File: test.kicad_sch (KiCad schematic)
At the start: 85 parts

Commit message: added symmetric voltage and input stage
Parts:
- added U?: LM27762, Package_SON:WSON-12-1EP_3x2mm_P0.5mm_EP1x2.65_ThermalVias, symbol Regulator_SwitchedCapacitor:LM27762
- C1, C2, C4: value (none) -> 1u; footprint (none) -> Capacitor_SMD:C_0805_2012Metric_Pad1.18x1.45mm_HandSolder
- C10, C11, C12, C13, C16, C17, C22, C23, C26, C27, C8, C9: value (none) -> 10u; footprint (none) -> Capacitor_SMD:C_0805_2012Metric_Pad1.18x1.45mm_HandSolder
- C14, C15, C18, C19, C20, C21, C24, C25, C28, C29, C7: value (none) -> 0.1u; footprint (none) -> Capacitor_SMD:C_0805_2012Metric_Pad1.18x1.45mm_HandSolder
- C3, C6: value (none) -> 4u7; footprint (none) -> Capacitor_SMD:C_0805_2012Metric_Pad1.18x1.45mm_HandSolder
- C30: value (none) -> 25p var; footprint (none) -> project_library:JZ300
- C31: value (none) -> 47n; footprint (none) -> Capacitor_SMD:C_0805_2012Metric_Pad1.18x1.45mm_HandSolder
- C32, C33: value (none) -> 100n; footprint (none) -> Capacitor_SMD:C_0805_2012Metric_Pad1.18x1.45mm_HandSolder
- C34: value (none) -> 1p; footprint (none) -> Capacitor_SMD:C_0805_2012Metric_Pad1.18x1.45mm_HandSolder
- C35: value (none) -> 5.5p-30p var; footprint (none) -> project_library:JZ300
- C5: value (none) -> 22u; footprint (none) -> Capacitor_SMD:C_0805_2012Metric_Pad1.18x1.45mm_HandSolder
- D1: value (none) -> LOW_BATTERY; footprint (none) -> LED_SMD:LED_0805_2012Metric_Pad1.15x1.40mm_HandSolder
- D2: value (none) -> LED_ValidSource; footprint (none) -> LED_SMD:LED_0805_2012Metric_Pad1.15x1.40mm_HandSolder
- D3: value (none) -> LED_Charging; footprint (none) -> LED_SMD:LED_0805_2012Metric_Pad1.15x1.40mm_HandSolder
- IC1: value (none) -> LC709203FQH-01TWG
- IC2: value (none) -> BQ24074RGTR
- IC3: value (none) -> USBLC6-2SC6
- IC4: value (none) -> ESP32-S3-WROOM-1-N16
- IC5, IC6: value (none) -> MCP6S91-E_MS
- IC7, IC8: value (none) -> MCP4726A1T-E_CH
- J1: value (none) -> UART0; footprint (none) -> Connector_PinHeader_2.54mm:PinHeader_1x04_P2.54mm_Vertical
- J2, J3: value (none) -> 73100-0105
- JP1: value (none) -> Jumper_3_Open; footprint (none) -> Connector_PinHeader_2.54mm:PinHeader_1x03_P2.54mm_Vertical
- K1, K2: value (none) -> AQY210EHA
- R1, R7, R8: value (none) -> 1k5; footprint (none) -> Resistor_SMD:R_0805_2012Metric_Pad1.20x1.40mm_HandSolder
- R10: value (none) -> 39; footprint (none) -> Resistor_SMD:R_0805_2012Metric_Pad1.20x1.40mm_HandSolder
- R11, R13: value (none) -> 5k; footprint (none) -> Resistor_SMD:R_0805_2012Metric_Pad1.20x1.40mm_HandSolder
- R12: value (none) -> 120; footprint (none) -> Resistor_SMD:R_0805_2012Metric_Pad1.20x1.40mm_HandSolder
- R14, R15: value (none) -> 470; footprint (none) -> Resistor_SMD:R_0805_2012Metric_Pad1.20x1.40mm_HandSolder
- R16, R17, R2, R4, R9: value (none) -> 5k1; footprint (none) -> Resistor_SMD:R_0805_2012Metric_Pad1.20x1.40mm_HandSolder
- R18, R19, R5: value (none) -> 1k; footprint (none) -> Resistor_SMD:R_0805_2012Metric_Pad1.20x1.40mm_HandSolder
- R20, R21: value (none) -> 165k; footprint (none) -> Resistor_SMD:R_0805_2012Metric_Pad1.20x1.40mm_HandSolder
- R22, R23: value (none) -> 835k; footprint (none) -> Resistor_SMD:R_0805_2012Metric_Pad1.20x1.40mm_HandSolder
- R3: value (none) -> 10k; footprint (none) -> Resistor_SMD:R_0805_2012Metric_Pad1.20x1.40mm_HandSolder
- R6: value (none) -> 820; footprint (none) -> Resistor_SMD:R_0805_2012Metric_Pad1.20x1.40mm_HandSolder
- SW1: value (none) -> Reset; footprint (none) -> project_library:SW_TS-1187A-B-A-B
- SW2: value (none) -> Boot
- U1, U2: value (none) -> 1043
- U3: value (none) -> USB-TYPE-C-018
- U4, U5, U6: value (none) -> LD1086DT33TR
- U7, U8: value (none) -> ADC08351CILQX/NOPB
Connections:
- net at C32.1, K1.3 (SW): now also J2.3; no longer C34.2, R22.2
- net at C32.2, K1.4 (SW): now also C34.1, R22.1; no longer C30.1, R20.1
- new net: C30.1, C34.2, R20.1, R22.2
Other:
- moved on the sheet: C32, C34, K1, R18, R22

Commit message: changed analog
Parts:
- removed C30: 25p var, project_library:JZ300, symbol Device:C_Small
- removed C32: 100n, Capacitor_SMD:C_0805_2012Metric_Pad1.18x1.45mm_HandSolder, symbol Device:C_Small
- removed C34: 1p, Capacitor_SMD:C_0805_2012Metric_Pad1.18x1.45mm_HandSolder, symbol Device:C_Small
- removed J2: 73100-0105, 73100-0105, symbol project_library:73100-0105
- removed K1: AQY210EHA, project_library:AQY210EHAX, symbol project_library:AQY210EHA
- removed R18: 1k, Resistor_SMD:R_0805_2012Metric_Pad1.20x1.40mm_HandSolder, symbol Device:R_Small
- removed R20: 165k, Resistor_SMD:R_0805_2012Metric_Pad1.20x1.40mm_HandSolder, symbol Device:R_Small
- removed R22: 835k, Resistor_SMD:R_0805_2012Metric_Pad1.20x1.40mm_HandSolder, symbol Device:R_Small
- removed U?: LM27762, Package_SON:WSON-12-1EP_3x2mm_P0.5mm_EP1x2.65_ThermalVias, symbol Regulator_SwitchedCapacitor:LM27762
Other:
- added sheet analog (analog.kicad_sch)

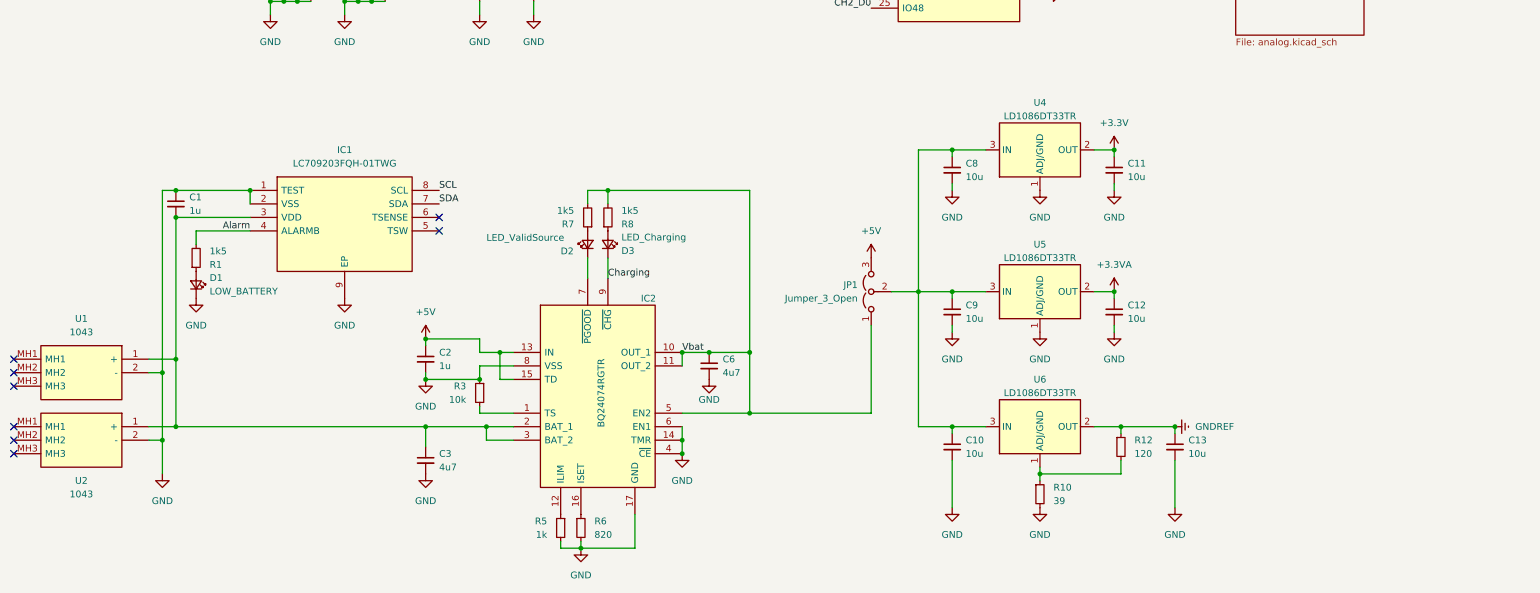
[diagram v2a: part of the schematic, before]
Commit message: Changed Power Suply to seperate sheet and added changed parts
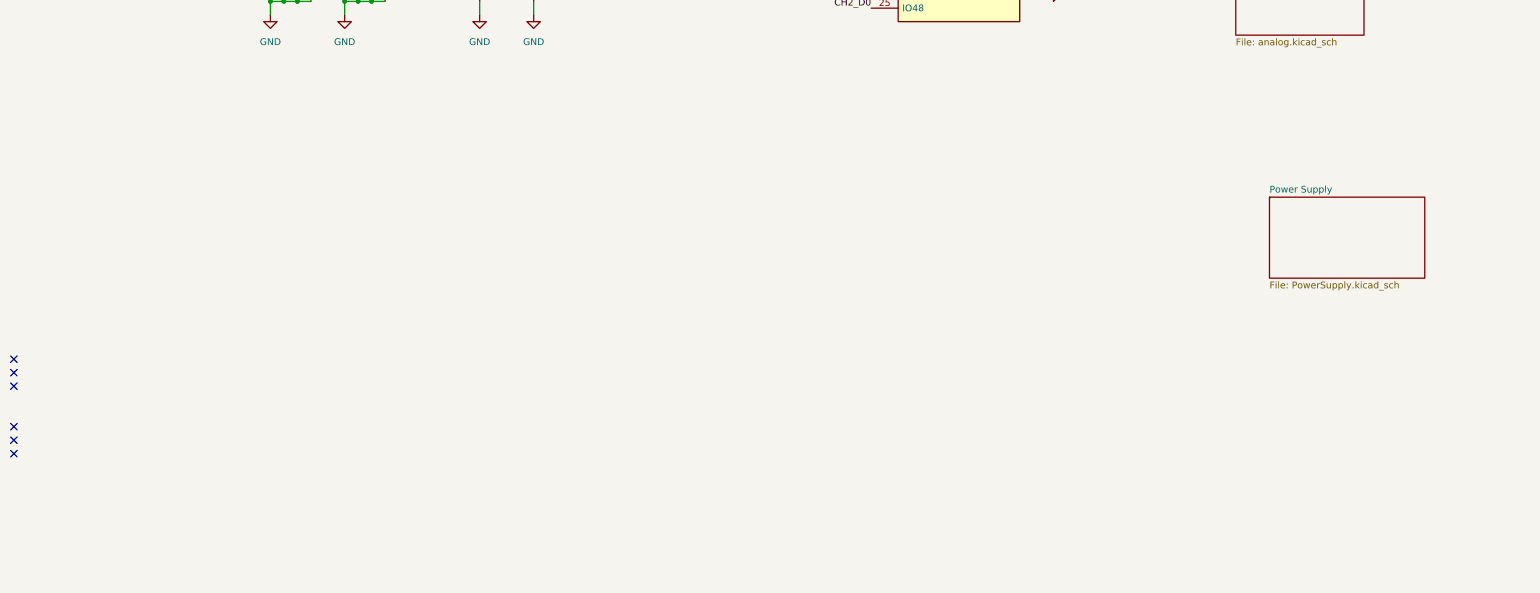
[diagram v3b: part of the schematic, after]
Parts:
- removed C1, C2: 1u, Capacitor_SMD:C_0805_2012Metric_Pad1.18x1.45mm_HandSolder, symbol Device:C_Small
- removed C10, C11, C12, C13, C8, C9: 10u, Capacitor_SMD:C_0805_2012Metric_Pad1.18x1.45mm_HandSolder, symbol Device:C_Small
- removed C3, C6: 4u7, Capacitor_SMD:C_0805_2012Metric_Pad1.18x1.45mm_HandSolder, symbol Device:C_Small
- removed D1: LOW_BATTERY, LED_SMD:LED_0805_2012Metric_Pad1.15x1.40mm_HandSolder, symbol Device:LED_Small
- removed D2: LED_ValidSource, LED_SMD:LED_0805_2012Metric_Pad1.15x1.40mm_HandSolder, symbol Device:LED_Small
- removed D3: LED_Charging, LED_SMD:LED_0805_2012Metric_Pad1.15x1.40mm_HandSolder, symbol Device:LED_Small
- removed IC1: LC709203FQH-01TWG, project_library:LC709203FQH-01TWG, symbol project_library:LC709203FQH-01TWG
- removed IC2: BQ24074RGTR, project_library:BQ24074RGTR, symbol project_library:BQ24074RGTR
- removed JP1: Jumper_3_Open, Connector_PinHeader_2.54mm:PinHeader_1x03_P2.54mm_Vertical, symbol Jumper:Jumper_3_Open
- removed R1, R7, R8: 1k5, Resistor_SMD:R_0805_2012Metric_Pad1.20x1.40mm_HandSolder, symbol Device:R_Small
- removed R10: 39, Resistor_SMD:R_0805_2012Metric_Pad1.20x1.40mm_HandSolder, symbol Device:R_Small
- removed R12: 120, Resistor_SMD:R_0805_2012Metric_Pad1.20x1.40mm_HandSolder, symbol Device:R_Small
- removed R3: 10k, Resistor_SMD:R_0805_2012Metric_Pad1.20x1.40mm_HandSolder, symbol Device:R_Small
- removed R5: 1k, Resistor_SMD:R_0805_2012Metric_Pad1.20x1.40mm_HandSolder, symbol Device:R_Small
- removed R6: 820, Resistor_SMD:R_0805_2012Metric_Pad1.20x1.40mm_HandSolder, symbol Device:R_Small
- removed U1, U2: 1043, project_library:1043, symbol project_library:1043
- removed U4, U5, U6: LD1086DT33TR, Package_TO_SOT_SMD:TO-252-2, symbol Regulator_Linear:LD1086DT33TR
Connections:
- no-connect marks 25 -> 23
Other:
- added sheet Power Supply (PowerSupply.kicad_sch)

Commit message: changed global labels, and delete analog file to solve merge
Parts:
- removed C24, C25, C28, C29: 0.1u, Capacitor_SMD:C_0805_2012Metric_Pad1.18x1.45mm_HandSolder, symbol Device:C_Small
- removed C26, C27: 10u, Capacitor_SMD:C_0805_2012Metric_Pad1.18x1.45mm_HandSolder, symbol Device:C_Small
- removed C31: 47n, Capacitor_SMD:C_0805_2012Metric_Pad1.18x1.45mm_HandSolder, symbol Device:C_Small
- removed C33: 100n, Capacitor_SMD:C_0805_2012Metric_Pad1.18x1.45mm_HandSolder, symbol Device:C_Small
- removed C35: 5.5p-30p var, project_library:JZ300, symbol Device:C_Small
- removed IC5, IC6: MCP6S91-E_MS, project_library:MCP6S91-E_MS, symbol project_library:MCP6S91-E_MS
- removed IC7, IC8: MCP4726A1T-E_CH, project_library:MCP4726A1T-E_CH, symbol project_library:MCP4726A1T-E_CH
- removed J3: 73100-0105, 73100-0105, symbol project_library:73100-0105
- removed K2: AQY210EHA, project_library:AQY210EHAX, symbol project_library:AQY210EHA
- removed R16, R17: 5k1, Resistor_SMD:R_0805_2012Metric_Pad1.20x1.40mm_HandSolder, symbol Device:R_Small
- removed R19: 1k, Resistor_SMD:R_0805_2012Metric_Pad1.20x1.40mm_HandSolder, symbol Device:R_Small
- removed R21: 165k, Resistor_SMD:R_0805_2012Metric_Pad1.20x1.40mm_HandSolder, symbol Device:R_Small
- removed R23: 835k, Resistor_SMD:R_0805_2012Metric_Pad1.20x1.40mm_HandSolder, symbol Device:R_Small
- added D?: (no value), LED_SMD:LED_0805_2012Metric_Pad1.15x1.40mm_HandSolder, symbol Device:LED_Small
- added JP?: (no value), symbol Jumper:Jumper_2_Bridged
- added R?: 1k5, Resistor_SMD:R_0805_2012Metric_Pad1.20x1.40mm_HandSolder, symbol Device:R_Small
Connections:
- net CS_A is gone; now on net CH2_Gnd_Sel: IC4.33 (IO40)
- net Charging is gone; now on net CH2_Gnd_Sel: IC4.35 (IO42)
- net +3.3VA: now also U7.14 (Vref)
- net CH1_Gnd_Sel: now also IC4.32 (IO39); no longer IC4.31 (IO38)
- net CH2_Gnd_Sel: no longer IC4.32 (IO39)
- net GND: now also D?.1 (K)
- net D+: now reaches IC3.4 (I/O2_2), U3.A6 (D+), U3.B6 (D+)
- net D-: now reaches IC3.6 (I/O1_2), U3.A7 (D-), U3.B7 (D-)
- net Status_PWM: now reaches IC4.28 (IO35)
- net Status_PWM: now also JP?.1 (A)
- net Trigger_Ref: now reaches IC4.29 (IO36)
- net Trigger_CH1: now reaches IC4.30 (IO37)
- net Analog_Out_CH2: now reaches U8.17 (VIN)
- net CS_B renamed CS_Gain
- new net: JP?.2 (B), R?.2
- new net: D?.2 (A), R?.1
- new net Trigger_CH2: IC4.31 (IO38)
- no-connect marks 23 -> 18
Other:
- removed sheet analog
- note removed: "16V ? Welcher R?"
- note removed: "Ax Serie bedeutet I2C-Adresse unterschiedliche bestellen"
- note removed: "PSRAM (S.11)"
- moved on the sheet: C14, C15, C16, C17, C18, C19, C20, C21, C22, C23, C4, C5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
